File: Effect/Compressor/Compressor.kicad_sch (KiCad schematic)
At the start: 43 parts, among them J1 Conn_01x04_Pin, J2 Conn_01x04_Pin, Q1 MMBF5103, Q2 DMMT5551, Q3 MMBF5103

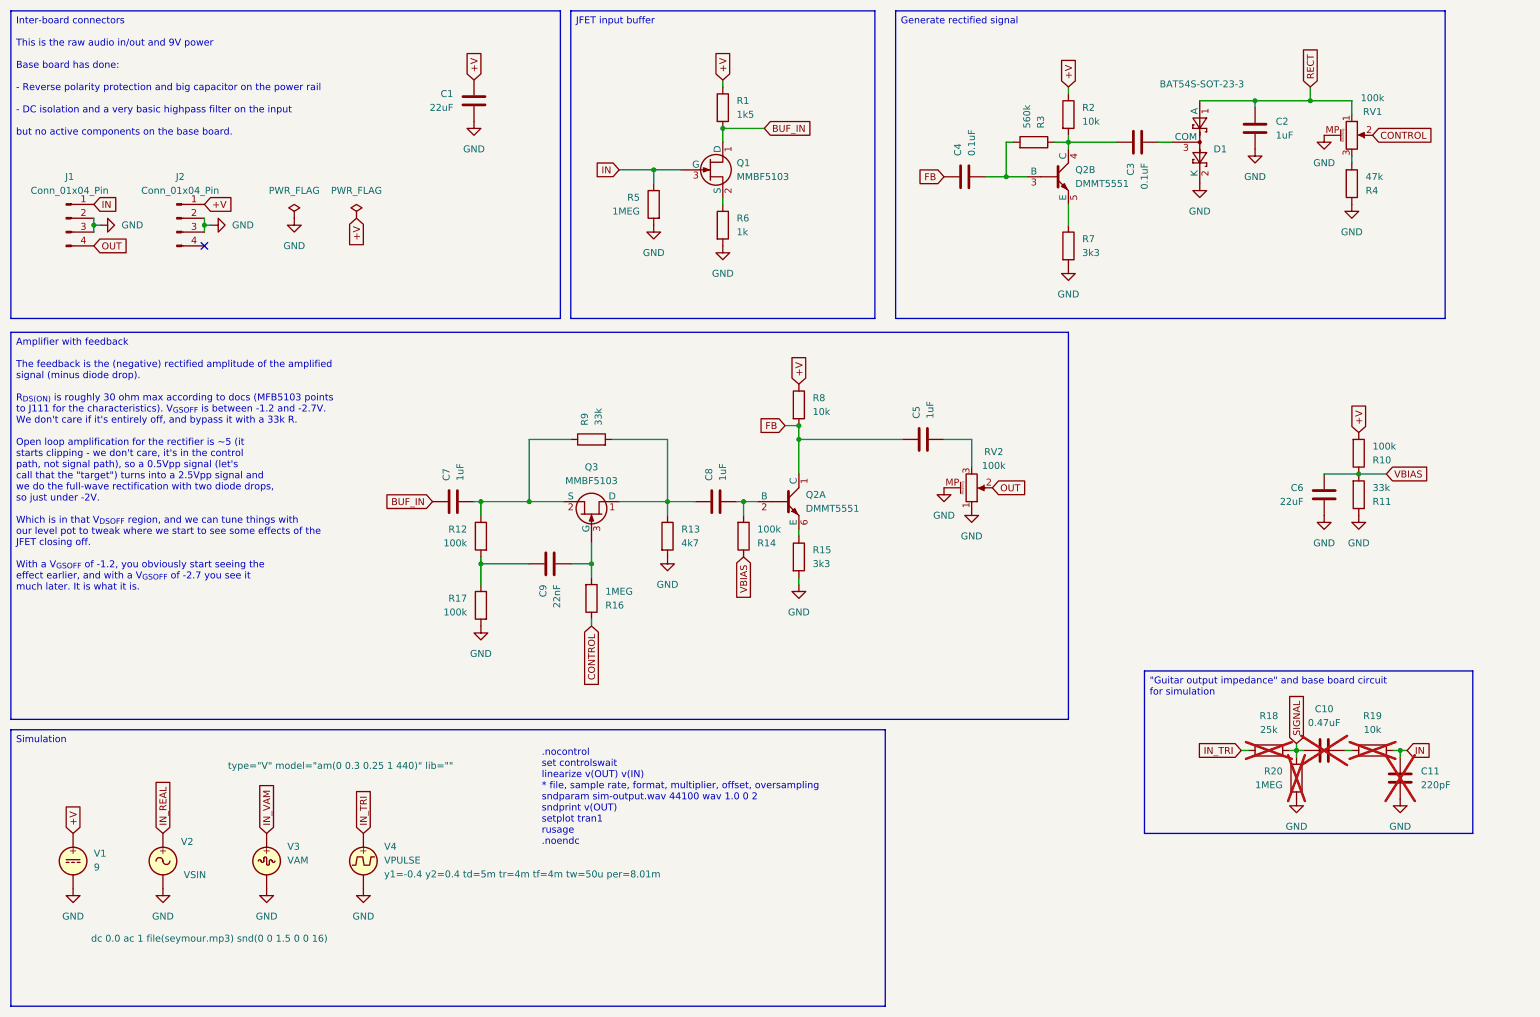
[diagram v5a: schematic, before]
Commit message: More compressor updates: add pots for attack / decay tuning etc
Lots of minor changes, but the user-visible one is that there is
(limited) control of the attack and delay now.  But the whole compressor
level setup has also changed, and the signal amplification is done a bit
differently too using the NPN/PNP pair in the NMB2227A.

Can you say "trying out random things"? I knew you could.

Let's get this manufactured and see if it actually works, since I won't
have time to mess with the design any more as the merge window opens and
my travel season starts.

Signed-off-by: Linus Torvalds <torvalds@linux-foundation.org>
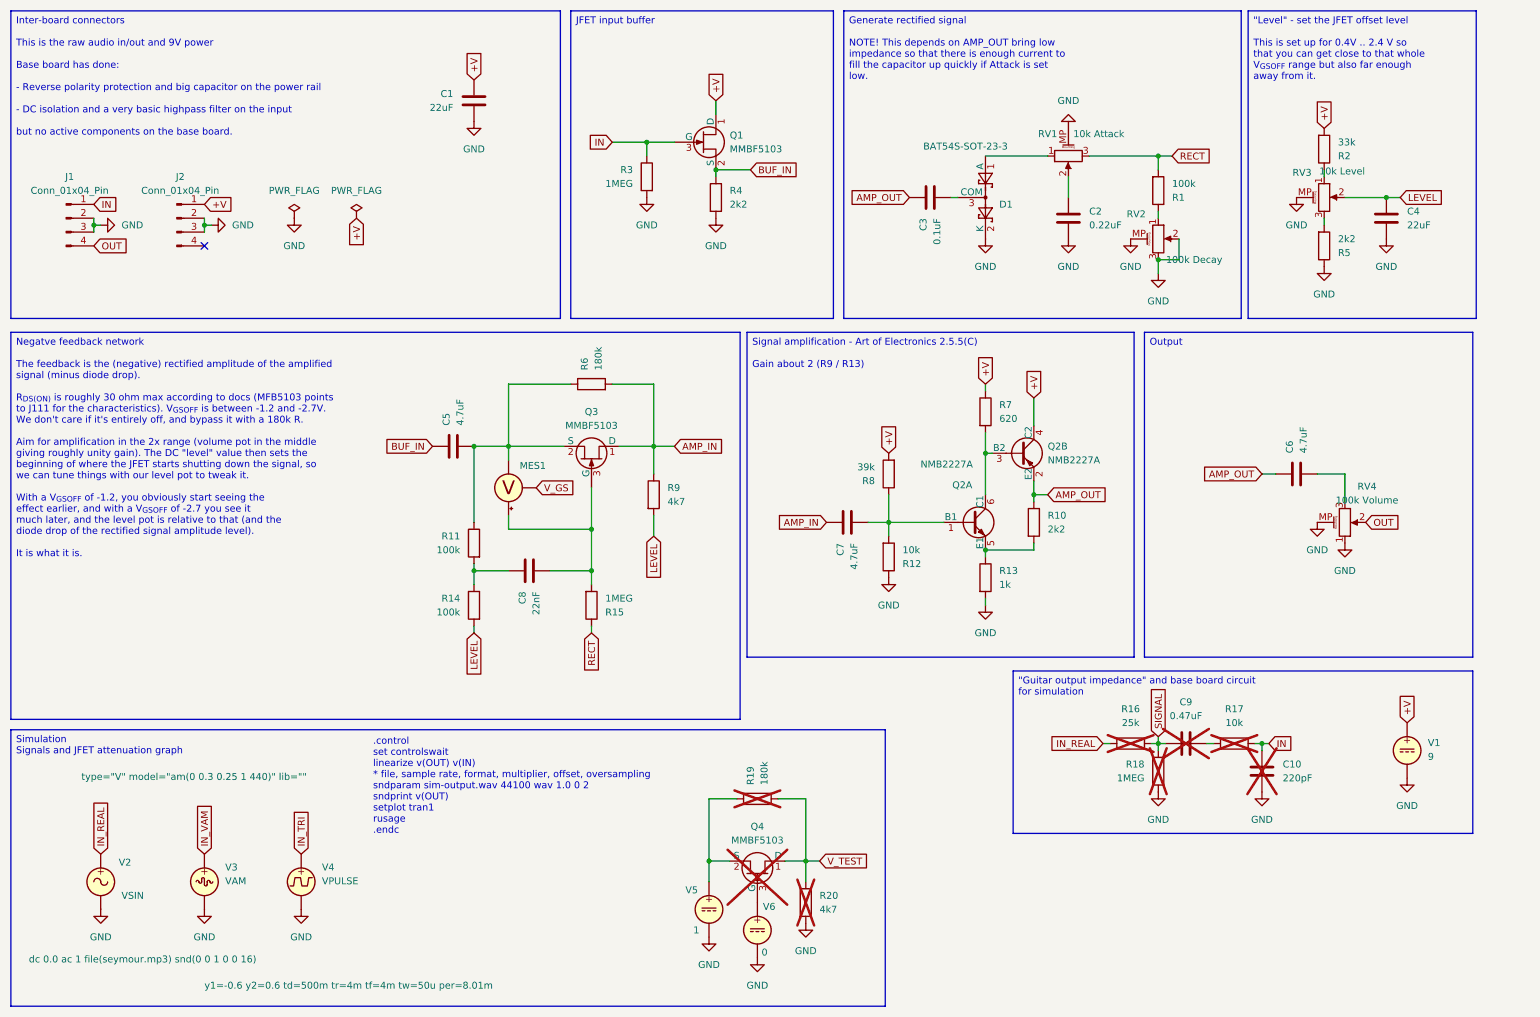
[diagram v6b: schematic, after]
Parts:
- removed C6: 22uF, Capacitor_SMD:C_1206_3216Metric, symbol Device:C
- removed Q2: DMMT5551, Package_TO_SOT_SMD:SOT-23-6, symbol Mylib:DMMT5551
- removed R11: 33k, Resistor_SMD:R_0805_2012Metric, symbol Device:R
- removed R14: 100k, Resistor_SMD:R_0805_2012Metric, symbol Device:R
- removed R3: 560k, Resistor_SMD:R_0805_2012Metric, symbol Device:R
- removed R4: 47k, Resistor_SMD:R_0805_2012Metric, symbol Device:R
- removed R8: 10k, Resistor_SMD:R_0805_2012Metric, symbol Device:R
- added MES1: VOLTMETER_DIFF, symbol Simulation_SPICE:VOLTMETER_DIFF
- added Q2: NMB2227A, Package_SO:TSOP-6_1.65x3.05mm_P0.95mm, symbol Mylib:NMB2227A
- added Q4: MMBF5103, Package_TO_SOT_SMD:SOT-23, symbol Mylib:MMBF5103
- added R10, R5: 2k2, Resistor_SMD:R_0805_2012Metric, symbol Device:R
- added R12: 10k, Resistor_SMD:R_0805_2012Metric, symbol Device:R
- added R19: 180k, Resistor_SMD:R_0805_2012Metric, symbol Device:R
- added R20: 4k7, Resistor_SMD:R_0805_2012Metric, symbol Device:R
- added RV2: 100k Decay, Mylib:Potentiometer_9mm_MP, symbol Device:R_Potentiometer_MountingPin
- added RV3: 10k Level, Mylib:Potentiometer_9mm_MP, symbol Device:R_Potentiometer_MountingPin
- added V5: 1, symbol Simulation_SPICE:VDC
- added V6: 0, symbol Simulation_SPICE:VDC
- C2: value 1uF -> 0.22uF
- C4: value 0.1uF -> 22uF; footprint Mylib:C_0704_1810Metric -> Capacitor_SMD:C_1206_3216Metric
- C5: renamed from C7; value 1uF -> 4.7uF
- C6: renamed from C5; value 1uF -> 4.7uF
- C7: renamed from C8; value 1uF -> 4.7uF
- R1: value 1k5 -> 100k
- R13: renamed from R15; value 3k3 -> 1k
- R2: value 10k -> 33k
- R4: renamed from R6; value 1k -> 2k2
- R6: renamed from R9; value 33k -> 180k
- R7: value 3k3 -> 620
- R8: renamed from R10; value 100k -> 39k
- RV1: value 100k -> 10k Attack
- RV4: renamed from RV2; value 100k -> 100k Volume
- renumbered C11 to C10, C9 to C8, C10 to C9, R12 to R11, R17 to R14, R16 to R15, R18 to R16, R19 to R17, R20 to R18, R5 to R3, R13 to R9
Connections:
- net VBIAS is gone; now on an unnamed net: R8.1
- net +V: now also Q1.1 (D), R2.2, R7.1, Q2.4 (C2); no longer R1.1, R2.1
- net BUF_IN: now also Q1.2 (S), R4.1; no longer Q1.1 (D), R1.2
- net GND: now also C4.2, R12.1, R20.2, R5.1, RV2.2, RV2.3, RV2.MP (MountPin), RV3.MP (MountPin), V5.2, V6.2; no longer R14.2, R7.2, R9.2
- net IN_REAL: now also R16.1
- net IN_TRI: no longer R16.1
- net RECT: now also R1.2, R15.1, RV1.3; no longer C2.1, D1.1 (A), RV1.1
- net AMP_OUT: now reaches C3.1
- net AMP_OUT: now also C6.1, Q2.2 (E2), R10.1; no longer R2.2
- net at C7.2: now also Q2.1 (B1), R12.2
- net at C5.2, Q3.2 (S), R11.1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: now also MES1.2 (-)
- net AMP_IN: now reaches C7.1, Q3.1 (D), R6.2, R9.1
- net at C8.2, Q3.3 (G), R15.2: now also MES1.1 (+)
- net at R13.1: now also Q2.5 (E1), R10.2
- net CONTROL: no longer names the net of RV1.2
- net CONTROL: now also C2.1; no longer R15.1
- net FB renamed LEVEL
- net LEVEL: now also R14.2, R9.2, RV3.2; no longer C6.1
- new net: Q2.3 (B2), Q2.6 (C1), R7.2
- new net: Q4.2 (S), R19.1, V5.1
- new net: Q4.3 (G), V6.1
- new net: R5.2, RV3.3
- new net: D1.1 (A), RV1.1
- new net: R1.1, RV2.1
- new net: R2.1, RV3.1
- new net V_GS: MES1.3 (out)
- new net V_TEST: Q4.1 (D), R19.2, R20.1
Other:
- note added: ".control set controlswait linearize v(OUT) v(IN) * file, sample rate, format, multiplier, offset, oversampling sndparam sim-output.wav 44100 wav 1.0 0 2 sndprint v(OUT) setplot tran1 rusage .endc"
- note removed: ".nocontrol set controlswait linearize v(OUT) v(IN) * file, sample rate, format, multiplier, offset, oversampling sndparam sim-output.wav 44100 wav 1.0 0 2 sndprint v(OUT) setplot tran1 rusage .noendc"
- moved on the sheet: C10, C2, C3, C5, C6, C7, C8, C9, D1, Q1, Q3, R11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

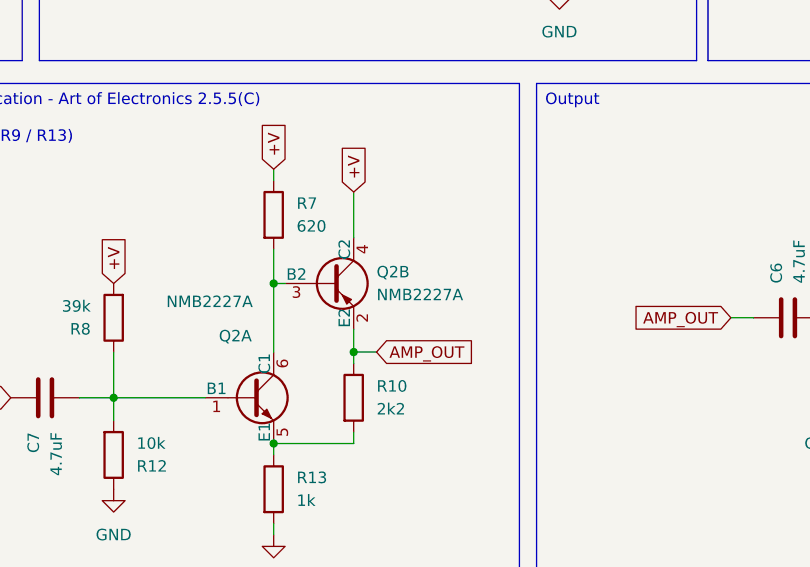
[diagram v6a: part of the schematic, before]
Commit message: Gaah - Fix stupid PNP direction mistake
I've done this *so* many times: I turn the PNP around by rotating it
like it's some random resistor, not my mirroring it around the Y-axis,
and I end up with the transistor the wrong way around without noticing
it.

And I did it *again*.

It didn't actually seem to matter for simulation, because this whole
"use a series pair" was just for the lulz and there wasn't any big
current or voltage gain expected.  And so the single NPN was perfectly
happy to drive it all.

But it's still very wrong indeed.

This just fixes the direction of the transistor, but I'll go look closer
if it had some unfortunate effect on the rest of my flawed results.

Signed-off-by: Linus Torvalds <torvalds@linux-foundation.org>
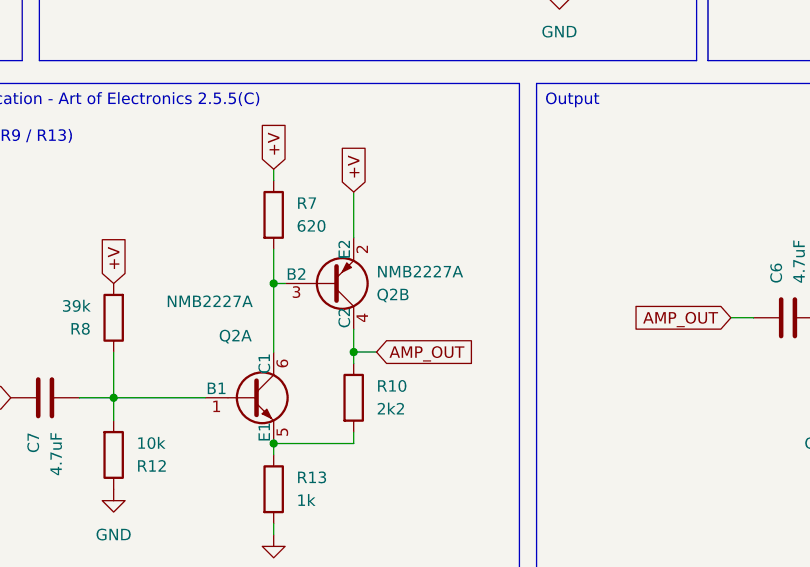
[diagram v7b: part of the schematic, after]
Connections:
- net +V: now also Q2.2 (E2); no longer Q2.4 (C2)
- net AMP_OUT: now also Q2.4 (C2); no longer Q2.2 (E2)
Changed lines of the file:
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@@
 		(lib_id "Mylib:NMB2227A")
 		(at 199.39 95.25 0)
+		(mirror x)
 		(unit 2)
 		(exclude_from_sim no)
@@
 		(on_board yes)
 		(dnp no)
-		(fields_autoplaced yes)
 		(property "Reference" "Q2"
-			(at 204.47 93.9799 0)
+			(at 204.47 96.5201 0)
 			(effects
 				(font
@@
 		)
 		(property "Value" "NMB2227A"
-			(at 204.47 96.5199 0)
+			(at 204.47 93.9801 0)
 			(effects
 				(font
@@
 		)
 		(property "Footprint" "Package_SO:TSOP-6_1.65x3.05mm_P0.95mm"
-			(at 199.39 107.95 0)
+			(at 199.39 82.55 0)
 			(hide yes)
 			(effects
@@
 		)
 		(property "Datasheet" "https://assets.nexperia.com/documents/data-sheet/NMB2227A.pdf"
-			(at 199.39 110.49 0)
+			(at 199.39 80.01 0)
 			(hide yes)
 			(effects
@@
 		)
 		(property "Description" "Dual NPN/PNP transistor, 6 pin package"
-			(at 200.406 81.534 0)
+			(at 200.406 108.966 0)
 			(hide yes)
 			(effects
@@
 		)
 		(property "Sim.Library" "/home/torvalds/KiCad/1590A/symbols/NMB2227A.lib"
-			(at 199.39 113.03 0)
+			(at 199.39 77.47 0)
 			(hide yes)
 			(effects
@@
 		)
 		(property "Sim.Name" "NMB2227A"
-			(at 198.12 115.57 0)
+			(at 198.12 74.93 0)
 			(hide yes)
 			(effects
@@
 		)
 		(property "Sim.Device" "SUBCKT"
-			(at 186.69 115.57 0)
+			(at 186.69 74.93 0)
 			(hide yes)
 			(effects
@@
 		)
 		(property "Sim.Pins" "1=B1 2=E2 3=B2 4=C2 5=E1 6=C1"
-			(at 200.66 115.57 0)
+			(at 200.66 74.93 0)
 			(hide yes)
 			(effects
